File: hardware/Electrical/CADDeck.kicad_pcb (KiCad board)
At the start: 2 copper layers, 129 x 82.5 mm, 44 parts, among them J1 Conn_01x05_Socket, J4 Conn_01x04_Socket, J5 Conn_01x10_Socket, Q1 2N2222, SW1 SW_Push, SW10 SW_Push, SW2 SW_Push, SW3 SW_Push, SW4 SW_Push, SW5 SW_Push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

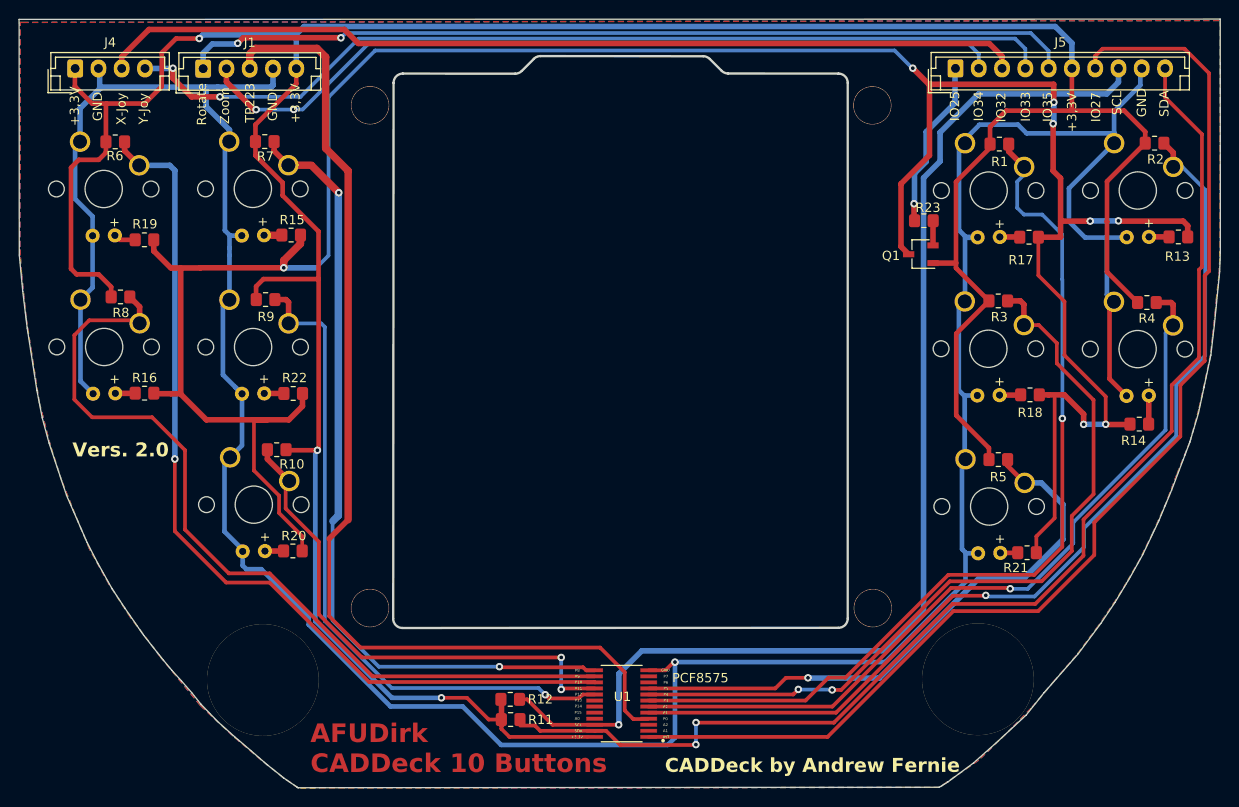
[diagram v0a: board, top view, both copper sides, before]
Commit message: Kondensatoren hinzugefügt
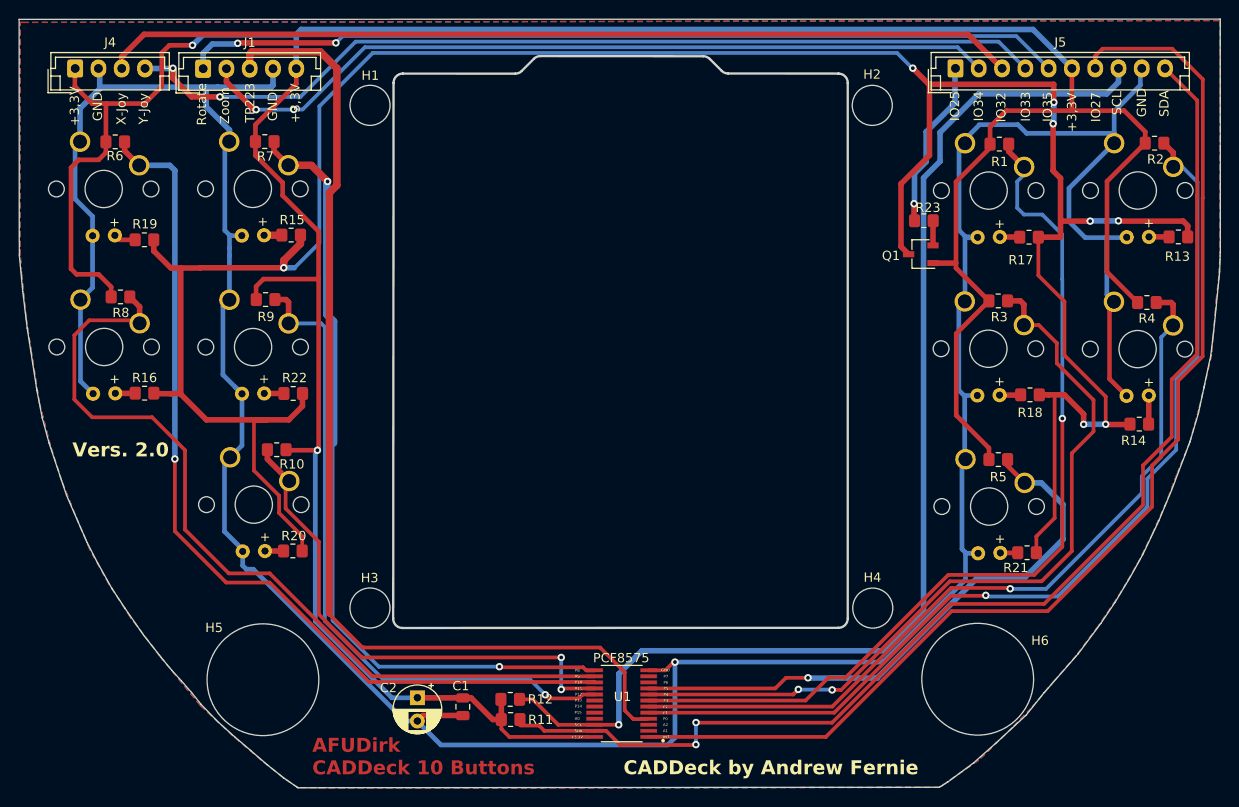
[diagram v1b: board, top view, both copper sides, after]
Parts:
- removed the H2 at (72.8, 25.9)
- removed the H2 at (126.7, 25.9)
- removed the H2 at (72.8, 79.9)
- removed the H2 at (126.8, 79.9)
- removed REF** (x2): MountingHole_12,0mm, Joystick:MountingHole_12.0mm
- added C1: 100nF, Capacitor_SMD:C_0805_2012Metric, F.Cu at (82.7, 90.5)
- added C2: 10uF/6V, Capacitor_THT:CP_Radial_D5.0mm_P2.50mm, F.Cu at (77.9, 89.5)
- added H1: MountingHole, MountingHole:MountingHole_4.3mm_M4, F.Cu at (72.8, 25.9)
- added H2: MountingHole, MountingHole:MountingHole_4.3mm_M4, F.Cu at (126.7, 25.9)
- added H3: MountingHole, MountingHole:MountingHole_4.3mm_M4, F.Cu at (72.8, 79.9)
- added H4: MountingHole, MountingHole:MountingHole_4.3mm_M4, F.Cu at (126.7, 79.9)
- added H5: MountingHole, MountingHole_12.0mm:MountingHole_8.4mm_M8, F.Cu at (61.3, 87.6)
- added H6: MountingHole, MountingHole_12.0mm:MountingHole_8.4mm_M8, F.Cu at (138.0, 87.6)
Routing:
- net Net-(J1-Pin_3): track 113.6 -> 120.3 mm
- net GND: track 334.0 -> 338.4 mm
- net +3.3V: track 352.5 -> 350.0 mm, vias 3 -> 2
- net Net-(Q1-C): track 284.1 -> 282.5 mm
- net Net-(J4-Pin_4): track 101.6 -> 100.1 mm
- net Net-(J1-Pin_1): track 96.0 -> 94.6 mm
- net Net-(J4-Pin_3): track 99.5 -> 98.3 mm
- net Net-(J1-Pin_2): track 88.4 -> 87.2 mm
- net Net-(U1-P02): track 85.0 -> 86.1 mm
- net Net-(U1-P01): track 105.4 -> 106.1 mm
- net Net-(J5-Pin_7): track 127.7 -> 127.0 mm

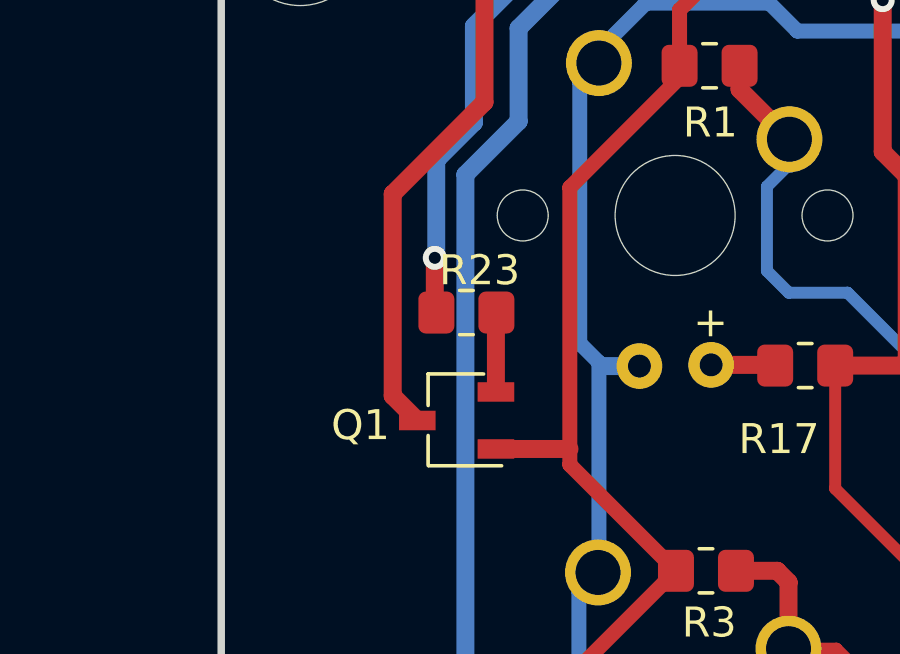
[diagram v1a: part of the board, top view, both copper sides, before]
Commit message: NPN durch PNP Transistor getauscht
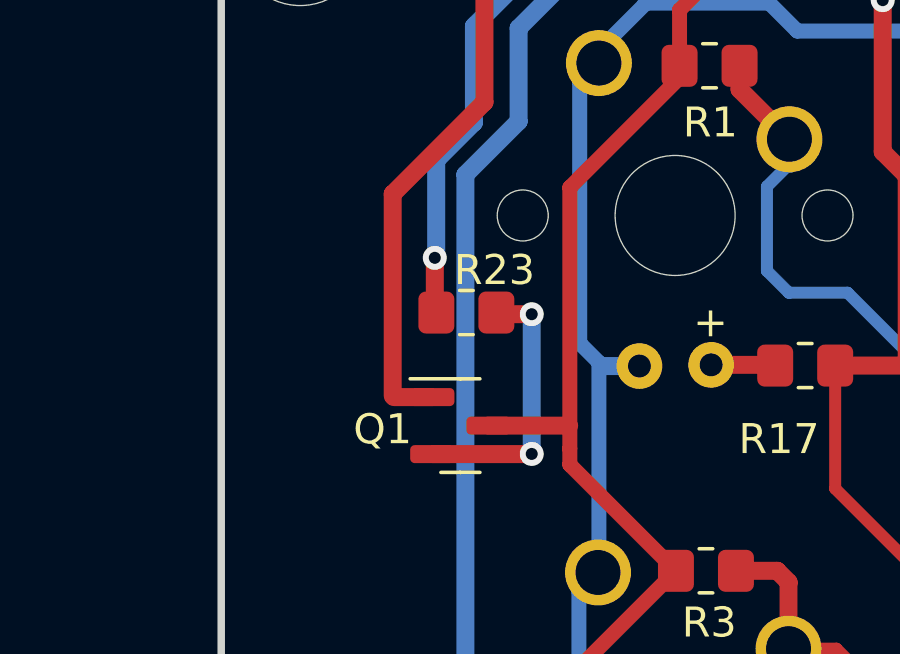
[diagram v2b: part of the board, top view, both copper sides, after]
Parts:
- H1, H2, H3, H4: value MountingHole -> MountingHole 4mm
- H5, H6: value MountingHole -> MountingHole 12mm
- Q1: value 2N2222 -> BC857; footprint Package_TO_SOT_SMD:TSOT-23 -> Package_TO_SOT_SMD:SOT-23
- moved Q1 0.21 mm to (132.0, 42.1), turned to 0 degrees
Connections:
- Q1 pad 1: +3.3V -> Net-(Q1-C)
- Q1 pad 3: Net-(Q1-C) -> +3.3V
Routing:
- net Net-(Q1-B): track 2.65 -> 9.20 mm, vias 0 -> 2

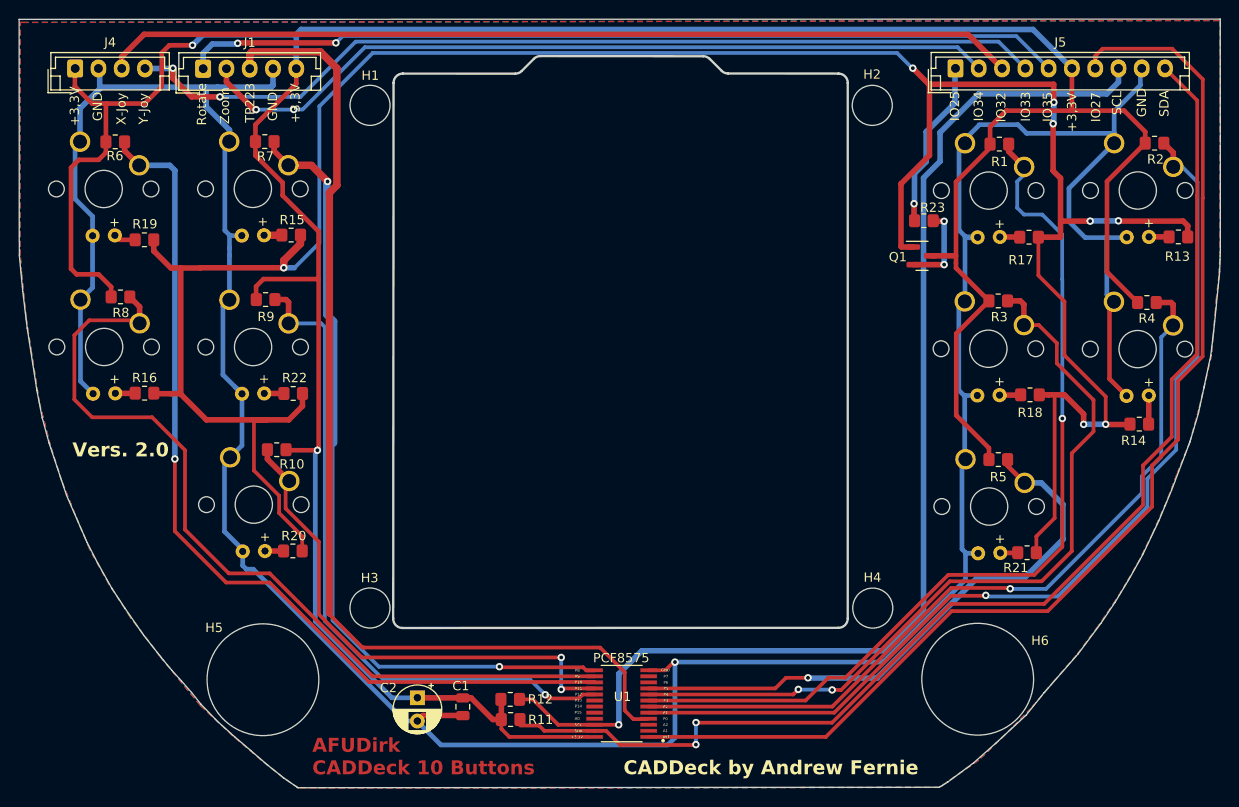
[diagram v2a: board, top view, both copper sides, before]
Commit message: LED Ansteuerung
hatte eine falsche Verbindung am Transistor
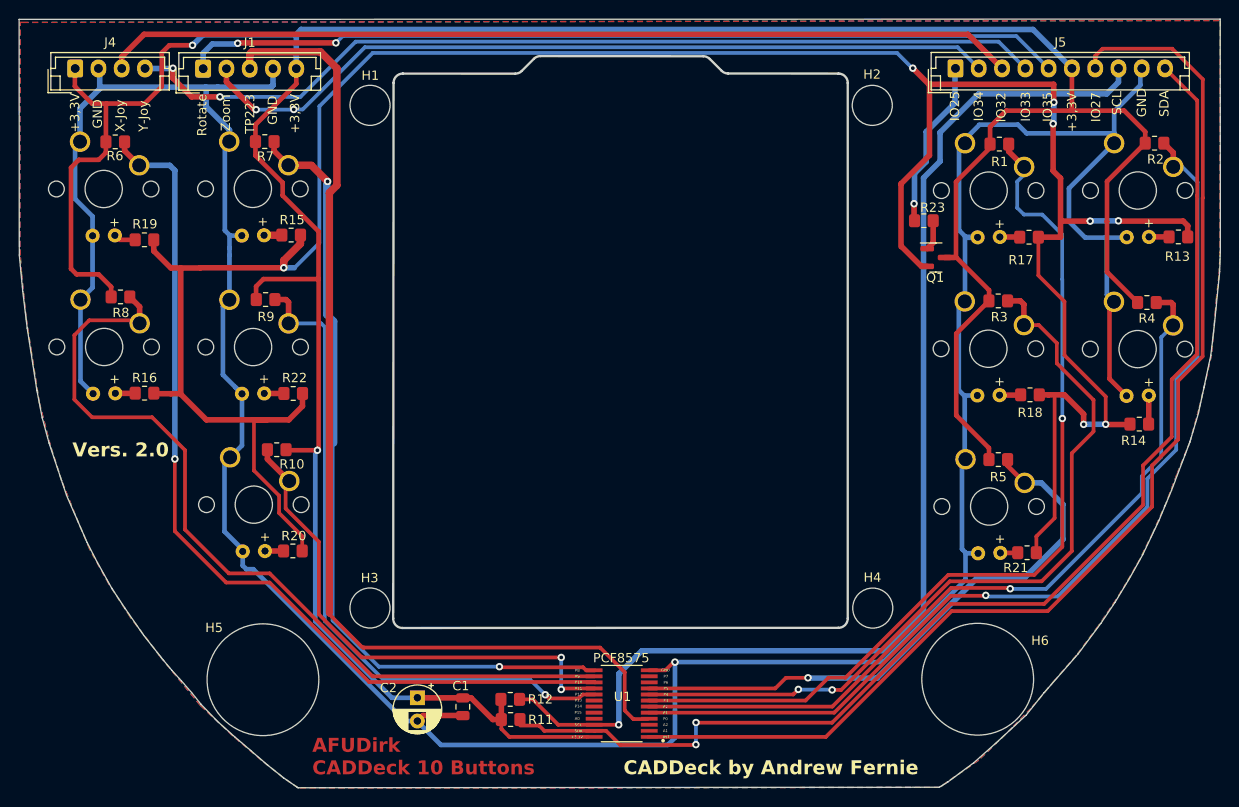
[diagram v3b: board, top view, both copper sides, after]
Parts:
- Q1: value BC857 -> 2N2222
- moved Q1 1.50 mm to (133.5, 42.3)
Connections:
- Q1 pad 1: Net-(Q1-C) -> Net-(Q1-B)
- Q1 pad 2: Net-(Q1-B) -> Net-(Q1-E)
- R13 pad 2: Net-(Q1-C) -> Net-(Q1-E)
- R14 pad 2: Net-(Q1-C) -> Net-(Q1-E)
- R15 pad 2: Net-(Q1-C) -> Net-(Q1-E)
- R16 pad 2: Net-(Q1-C) -> Net-(Q1-E)
- R17 pad 2: Net-(Q1-C) -> Net-(Q1-E)
- R18 pad 2: Net-(Q1-C) -> Net-(Q1-E)
- R19 pad 2: Net-(Q1-C) -> Net-(Q1-E)
- R20 pad 2: Net-(Q1-C) -> Net-(Q1-E)
- R21 pad 2: Net-(Q1-C) -> Net-(Q1-E)
- R22 pad 2: Net-(Q1-C) -> Net-(Q1-E)
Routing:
- net Net-(Q1-E): track 0.00 -> 285.0 mm, vias 0 -> 8
- net Net-(Q1-C): track 282.7 -> 0.00 mm, vias 8 -> 0
- net Net-(Q1-B): track 9.20 -> 3.29 mm, vias 2 -> 0
- net +3.3V: track 350.3 -> 348.6 mm

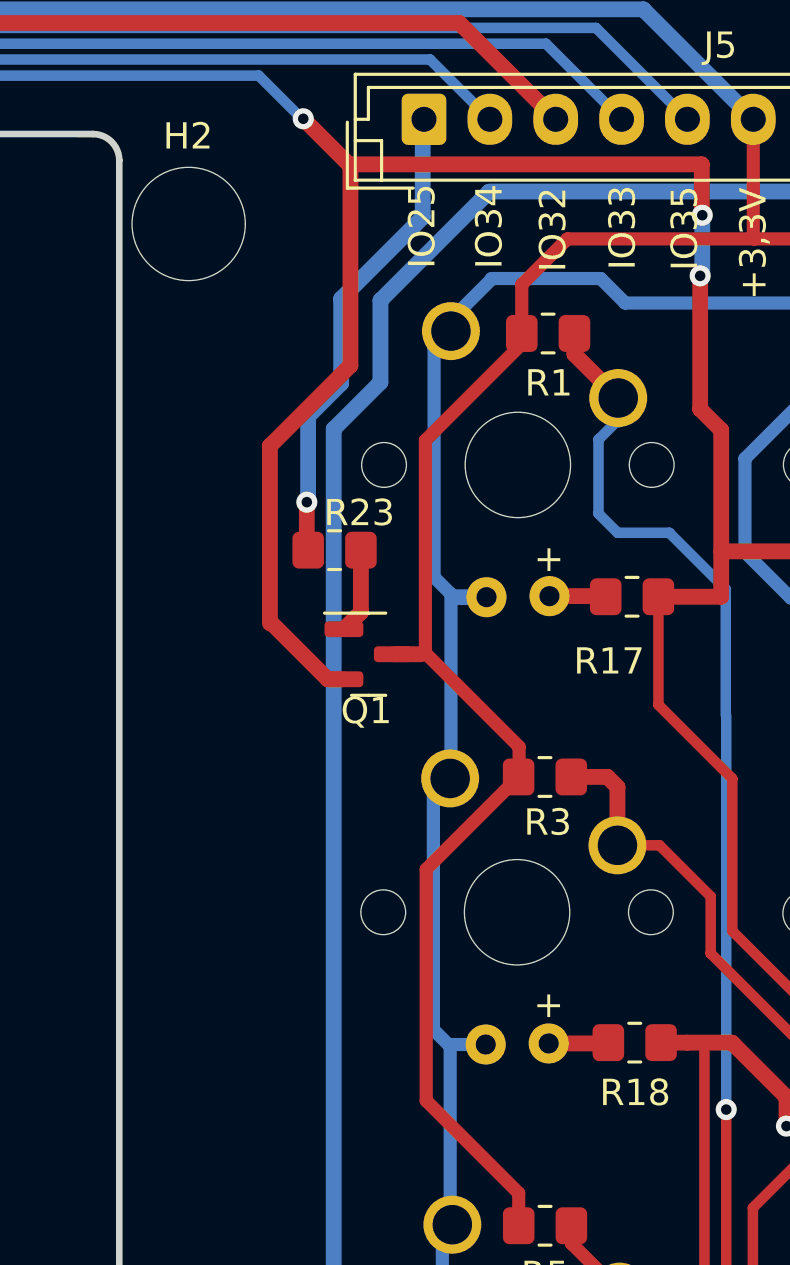
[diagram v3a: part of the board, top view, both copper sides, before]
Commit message: Transistor für LED Ansteuerung geändert
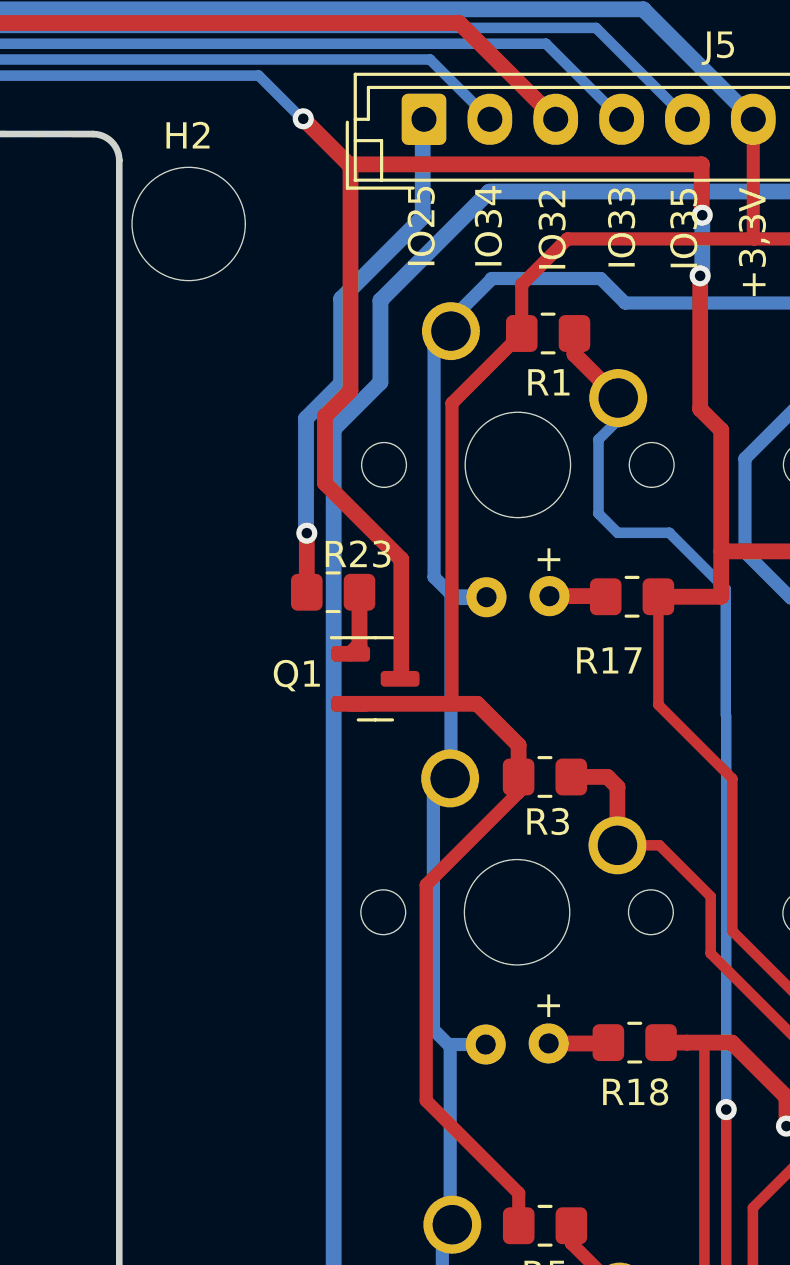
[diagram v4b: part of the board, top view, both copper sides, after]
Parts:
- Q1: value 2N2222 -> BC857
- moved R23 1.60 mm to (132.2, 39.9)
- moved Q1 0.97 mm to (133.8, 43.2)
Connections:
- Q1 pad 2: Net-(Q1-E) -> +3.3V
- Q1 pad 3: +3.3V -> Net-(Q1-C)
- R13 pad 2: Net-(Q1-E) -> Net-(Q1-C)
- R14 pad 2: Net-(Q1-E) -> Net-(Q1-C)
- R15 pad 2: Net-(Q1-E) -> Net-(Q1-C)
- R16 pad 2: Net-(Q1-E) -> Net-(Q1-C)
- R17 pad 2: Net-(Q1-E) -> Net-(Q1-C)
- R18 pad 2: Net-(Q1-E) -> Net-(Q1-C)
- R19 pad 2: Net-(Q1-E) -> Net-(Q1-C)
- R20 pad 2: Net-(Q1-E) -> Net-(Q1-C)
- R21 pad 2: Net-(Q1-E) -> Net-(Q1-C)
- R22 pad 2: Net-(Q1-E) -> Net-(Q1-C)
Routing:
- net Net-(Q1-E): track 285.0 -> 0.00 mm, vias 8 -> 0
- net Net-(Q1-C): track 0.00 -> 283.8 mm, vias 0 -> 8
- net +3.3V: track 348.6 -> 351.2 mm
- net Net-(J5-Pin_1): track 18.3 -> 19.9 mm
- net Net-(Q1-B): track 3.29 -> 2.47 mm

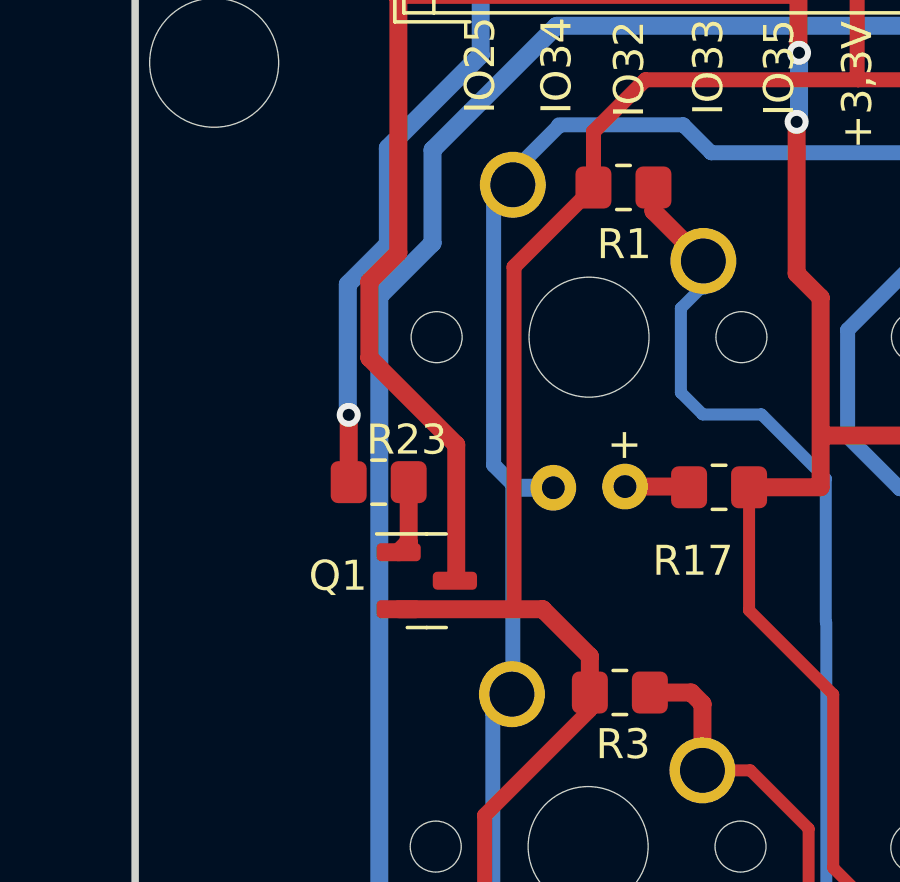
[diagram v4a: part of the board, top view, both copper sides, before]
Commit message: Transistor geändert
Bei KiCad war ein fehlerhafter Footprint.
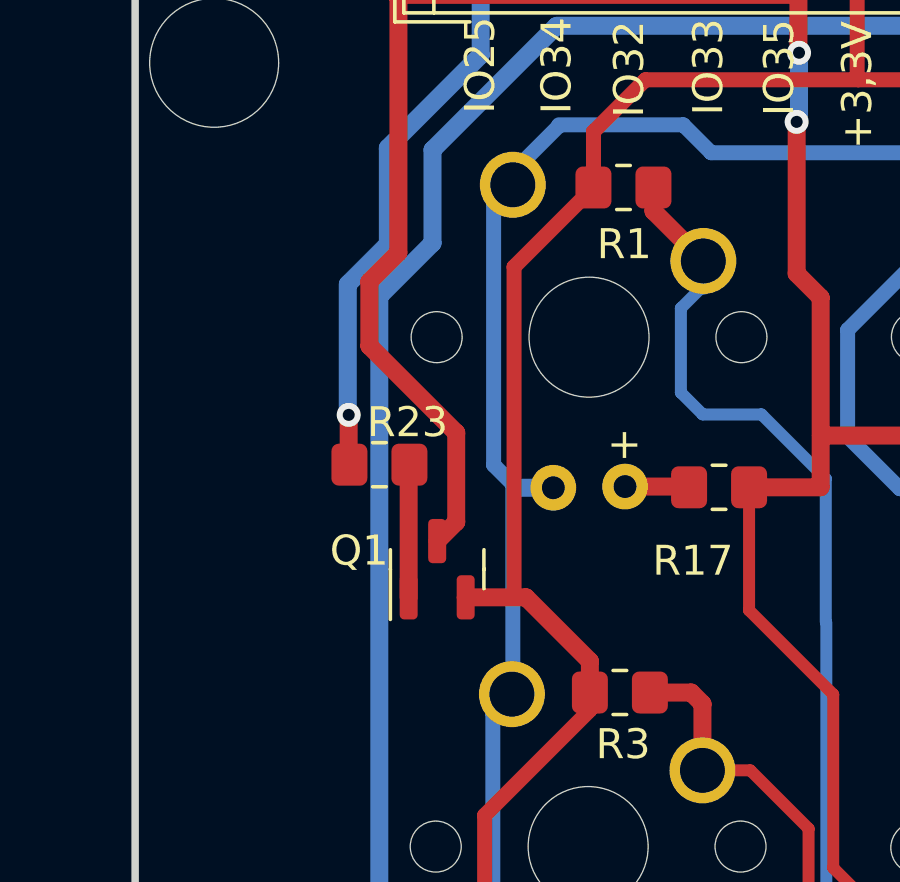
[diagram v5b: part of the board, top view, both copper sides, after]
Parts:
- Q1: value BC857 -> 2N2222
- moved R23 0.58 mm to (132.2, 39.3)
- moved Q1 0.52 mm to (134.1, 42.8), turned to 90 degrees
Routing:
- net +3.3V: track 351.2 -> 348.6 mm
- net Net-(Q1-B): track 2.47 -> 4.43 mm
- net Net-(Q1-C): track 283.8 -> 282.7 mm
- net Net-(J5-Pin_1): track 19.9 -> 19.3 mm
